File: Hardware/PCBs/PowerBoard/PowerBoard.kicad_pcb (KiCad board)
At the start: 2 copper layers, 24 parts, among them IC1 AZ34063UMTR-G1, IC2 LD29150DT33R, J1 Screw_Terminal_01x02, J2 Conn_01x04, J3 Screw_Terminal_01x02, J4 Conn_01x02, J5 Screw_Terminal_01x02, U1 L298HN

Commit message: PCB routed
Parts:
- added J6: Conn_01x02, Connector_PinSocket_2.54mm:PinSocket_1x02_P2.54mm_Vertical, F.Cu at (26.2, 76.6)
- IC1: footprint Package_SO:SOIC-8-1EP_3.9x4.9mm_P1.27mm_EP2.29x3mm_ThermalVias -> Package_SO:SOIC-8_3.9x4.9mm_P1.27mm
- IC2: footprint Package_TO_SOT_SMD:TO-252-2_TabPin1 -> Package_TO_SOT_SMD:TO-252-2
- moved L1 83.1 mm to (28.2, 56.6), turned to 180 degrees
- moved C5 77.0 mm to (34.9, 78.1), turned to 90 degrees
- moved C2 74.0 mm to (33.8, 55.0)
- moved Ctiming1 66.9 mm to (29.7, 61.6), turned to 180 degrees
- moved D3 65.9 mm to (37.1, 78.1), turned to 270 degrees
- moved C1 62.6 mm to (32.7, 68.0), turned to 180 degrees
- moved C4 61.9 mm to (54.7, 77.4), turned to 90 degrees
- moved Rsc1 58.2 mm to (42.0, 60.2), turned to 90 degrees
- moved R4 56.3 mm to (37.1, 73.6), turned to 90 degrees
- moved D2 54.5 mm to (55.0, 72.7)
- moved C3 48.9 mm to (55.8, 68.2), turned to 90 degrees
- moved J5 47.3 mm to (52.7, 56.6), turned to 180 degrees
- moved L2 45.7 mm to (48.8, 67.2)
- moved R2 43.3 mm to (37.1, 67.4), turned to 270 degrees
- moved U1 41.3 mm to (77.9, 74.6), turned to 180 degrees
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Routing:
- net GND: track 0.00 -> 147.2 mm
- net VCC: track 0.00 -> 74.8 mm, vias 0 -> 1
- net +3V3: track 0.00 -> 53.9 mm, vias 0 -> 1
- net Net-(J3-Pad2): track 0.00 -> 39.4 mm
- net Net-(J1-Pad1): track 0.00 -> 31.6 mm
- net Net-(J4-Pad2): track 0.00 -> 28.2 mm
- net +5V: track 0.00 -> 23.7 mm, vias 0 -> 1
- net +5F: track 0.00 -> 22.3 mm
- net Net-(J1-Pad2): track 0.00 -> 20.0 mm
- net Net-(J4-Pad1): track 0.00 -> 19.2 mm
- net Net-(J2-Pad4): track 0.00 -> 17.2 mm
- net Net-(J2-Pad2): track 0.00 -> 14.6 mm
- net Net-(J2-Pad3): track 0.00 -> 13.6 mm
- net Net-(D1-Pad2): track 0.00 -> 13.5 mm
- net Net-(J3-Pad1): track 0.00 -> 13.1 mm
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
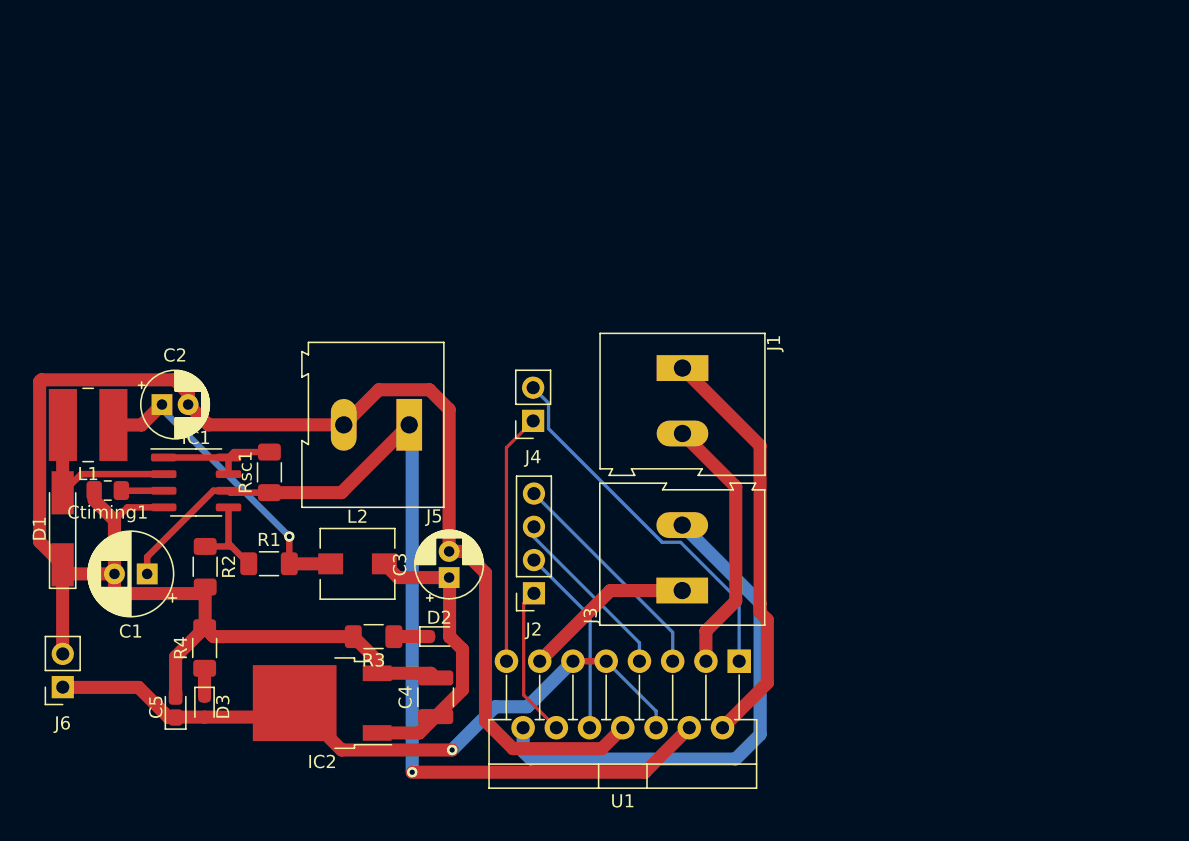
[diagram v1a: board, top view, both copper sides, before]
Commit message: Added ground planes and mounting holes
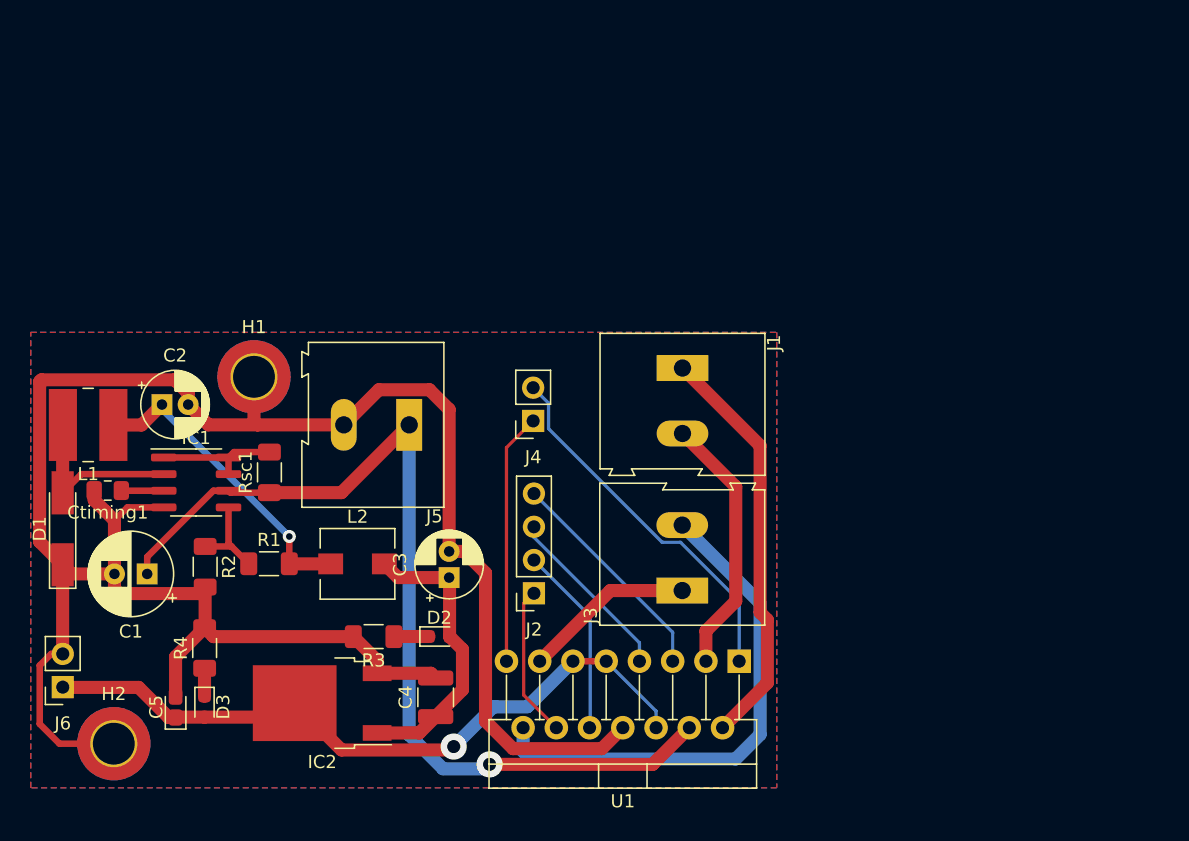
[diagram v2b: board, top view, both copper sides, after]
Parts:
- added H1: MountingHole_Pad, MountingHole:MountingHole_3.2mm_M3_DIN965_Pad_TopBottom, F.Cu at (40.9, 52.9)
- added H2: MountingHole_Pad, MountingHole:MountingHole_3.2mm_M3_DIN965_Pad_TopBottom, F.Cu at (30.1, 80.9)
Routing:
- net GND: track 147.2 -> 163.8 mm
- net VCC: track 74.8 -> 73.4 mm
- added copper zone on B.Cu, net GND
- added copper zone on F.Cu, net GND
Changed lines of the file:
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@@
   (general
     (thickness 1.6)
-    (drawings 0)
-    (tracks 145)
+    (drawings 6)
+    (tracks 160)
     (zones 0)
-    (modules 25)
+    (modules 27)
     (nets 22)
   )
@@
   )
   (setup
-    (last_trace_width 1)
+    (last_trace_width 0.5)
     (user_trace_width 0.5)
     (user_trace_width 1)
@@
     (via_min_size 0.4)
     (via_min_drill 0.3)
+    (user_via 1 0.5)
+    (user_via 2 1)
     (uvia_size 0.3)
     (uvia_drill 0.1)
@@
     (add_net "Net-(J4-Pad2)")
     (add_net VCC)
+  )
+  (module MountingHole:MountingHole_3.2mm_M3_DIN965_Pad_TopBottom (layer F.Cu)
+    (at 30.15 80.93)
+    (descr "Mounting Hole 3.2mm, M3, DIN965")
+    (tags "mounting hole 3.2mm m3 din965")
+    (attr virtual)
+    (fp_text reference H2 (at 0 -3.8) (layer F.SilkS)
+      (effects (font (size 1 1) (thickness 0.15)))
+    )
+    (fp_text value MountingHole_Pad (at 0 3.8) (layer F.Fab)
+      (effects (font (size 1 1) (thickness 0.15)))
+    )
+    (fp_text user %R (at 0.3 0) (layer F.Fab)
+      (effects (font (size 1 1) (thickness 0.15)))
+    )
+    (fp_circle (center 0 0) (end 2.8 0) (layer Cmts.User) (width 0.15))
+    (fp_circle (center 0 0) (end 3.05 0) (layer F.CrtYd) (width 0.05))
+    (pad 1 connect circle (at 0 0) (size 5.6 5.6) (layers B.Cu B.Mask)
+      (net 2 GND))
+    (pad 1 connect circle (at 0 0) (size 5.6 5.6) (layers F.Cu F.Mask)
+      (net 2 GND))
+    (pad 1 thru_hole circle (at 0 0) (size 3.6 3.6) (drill 3.2) (layers *.Cu *.Mask)
+      (net 2 GND))
+  )
+  (module MountingHole:MountingHole_3.2mm_M3_DIN965_Pad_TopBottom (layer F.Cu)
+    (at 40.86 52.9)
+    (descr "Mounting Hole 3.2mm, M3, DIN965")
+    (tags "mounting hole 3.2mm m3 din965")
+    (attr virtual)
+    (fp_text reference H1 (at 0 -3.8) (layer F.SilkS)
+      (effects (font (size 1 1) (thickness 0.15)))
+    )
+    (fp_text value MountingHole_Pad (at 0 3.8) (layer F.Fab)
+      (effects (font (size 1 1) (thickness 0.15)))
+    )
+    (fp_text user %R (at 0.3 0) (layer F.Fab)
+      (effects (font (size 1 1) (thickness 0.15)))
+    )
+    (fp_circle (center 0 0) (end 2.8 0) (layer Cmts.User) (width 0.15))
+    (fp_circle (center 0 0) (end 3.05 0) (layer F.CrtYd) (width 0.05))
+    (pad 1 connect circle (at 0 0) (size 5.6 5.6) (layers B.Cu B.Mask)
+      (net 2 GND))
+    (pad 1 connect circle (at 0 0) (size 5.6 5.6) (layers F.Cu F.Mask)
+      (net 2 GND))
+    (pad 1 thru_hole circle (at 0 0) (size 3.6 3.6) (drill 3.2) (layers *.Cu *.Mask)
+      (net 2 GND))
   )
   (module Connector_PinSocket_2.54mm:PinSocket_1x02_P2.54mm_Vertical (layer F.Cu)
@@
     )
   )
+  (gr_line (start 23.66 49.35) (end 81 49.35) (layer Dwgs.User) (width 0.15))
+  (gr_line (start 23.66 50.08) (end 23.66 49.35) (layer Dwgs.User) (width 0.15))
+  (gr_line (start 23.66 84.47) (end 23.66 50.08) (layer Dwgs.User) (width 0.15))
+  (gr_line (start 24.17 84.47) (end 23.66 84.47) (layer Dwgs.User) (width 0.15))
+  (gr_line (start 81 84.47) (end 24.17 84.47) (layer Dwgs.User) (width 0.15))
+  (gr_line (start 81 49.35) (end 81 84.47) (layer Dwgs.User) (width 0.15))
   (segment (start 47.54 61.75) (end 42.04 61.75) (width 1) (layer F.Cu) (net 1))
   (segment (start 52.72 56.57) (end 47.54 61.75) (width 1) (layer F.Cu) (net 1))
@@
   (segment (start 37.755 61.605) (end 38.915 61.605) (width 0.5) (layer F.Cu) (net 1))
   (segment (start 32.7 67.96) (end 32.7 66.66) (width 0.5) (layer F.Cu) (net 1))
-  (segment (start 74.12 79.71) (end 70.72 83.11) (width 1) (layer F.Cu) (net 1))
-  (segment (start 70.72 83.11) (end 52.95 83.11) (width 1) (layer F.Cu) (net 1))
-  (segment (start 52.95 83.11) (end 52.95 83.11) (width 1) (layer F.Cu) (net 1))
-  (via (at 52.95 83.11) (size 0.8) (drill 0.4) (layers F.Cu B.Cu) (net 1))
   (segment (start 52.95 56.8) (end 52.72 56.57) (width 1) (layer B.Cu) (net 1))
-  (segment (start 52.95 83.11) (end 52.95 56.8) (width 1) (layer B.Cu) (net 1))
+  (segment (start 71.319989 82.510011) (end 58.859989 82.510011) (width 1) (layer F.Cu) (net 1))
+  (segment (start 74.12 79.71) (end 71.319989 82.510011) (width 1) (layer F.Cu) (net 1))
+  (segment (start 58.859989 82.510011) (end 58.859989 82.510011) (width 1) (layer F.Cu) (net 1))
+  (via (at 58.859989 82.510011) (size 2) (drill 1) (layers F.Cu B.Cu) (net 1))
+  (segment (start 55.303999 82.850001) (end 58.519999 82.850001) (width 1) (layer B.Cu) (net 1))
+  (segment (start 58.519999 82.850001) (end 58.859989 82.510011) (width 1) (layer B.Cu) (net 1))
+  (segment (start 52.72 80.266002) (end 55.303999 82.850001) (width 1) (layer B.Cu) (net 1))
+  (segment (start 52.72 56.57) (end 52.72 80.266002) (width 1) (layer B.Cu) (net 1))
   (segment (start 37.38 56.57) (end 35.83 55.02) (width 1) (layer F.Cu) (net 2))
-  (segment (start 47.72 56.57) (end 37.38 56.57) (width 1) (layer F.Cu) (net 2))
   (segment (start 26.94 67.96) (end 26.24 67.26) (width 1) (layer F.Cu) (net 2))
   (segment (start 30.2 67.96) (end 26.94 67.96) (width 1) (layer F.Cu) (net 2))
@@
   (segment (start 56.90137 66.24) (end 58.549999 67.888629) (width 1) (layer F.Cu) (net 2))
   (segment (start 55.77 66.24) (end 56.90137 66.24) (width 1) (layer F.Cu) (net 2))
+  (segment (start 40.86 56.3) (end 41.13 56.57) (width 1) (layer F.Cu) (net 2))
+  (segment (start 40.86 52.9) (end 40.86 56.3) (width 1) (layer F.Cu) (net 2))
+  (segment (start 41.13 56.57) (end 37.38 56.57) (width 1) (layer F.Cu) (net 2))
+  (segment (start 47.72 56.57) (end 41.13 56.57) (width 1) (layer F.Cu) (net 2))
+  (segment (start 26 80.93) (end 30.15 80.93) (width 0.5) (layer F.Cu) (net 2))
+  (segment (start 24.49 79.42) (end 26 80.93) (width 0.5) (layer F.Cu) (net 2))
+  (segment (start 24.49 74.95) (end 24.49 79.42) (width 0.5) (layer F.Cu) (net 2))
+  (segment (start 25.37 74.07) (end 24.49 74.95) (width 0.5) (layer F.Cu) (net 2))
+  (segment (start 26.25 74.07) (end 25.37 74.07) (width 0.5) (layer F.Cu) (net 2))
   (segment (start 32.27 56.58) (end 33.83 55.02) (width 1) (layer F.Cu) (net 3))
   (segment (start 30.12 56.58) (end 32.27 56.58) (width 1) (layer F.Cu) (net 3))
@@
   (segment (start 43.56 67.18) (end 43.56 65.1) (width 0.5) (layer F.Cu) (net 3))
   (segment (start 43.56 65.1) (end 43.56 65.1) (width 0.5) (layer F.Cu) (net 3))
-  (via (at 43.56 65.1) (size 0.8) (drill 0.4) (layers F.Cu B.Cu) (net 3))
   (segment (start 33.83 55.37) (end 33.83 55.02) (width 0.5) (layer B.Cu) (net 3))
   (segment (start 43.56 65.1) (end 33.83 55.37) (width 0.5) (layer B.Cu) (net 3))
+  (segment (start 43.56 65.1) (end 43.56 65.1) (width 0.5) (layer F.Cu) (net 3))
+  (via (at 43.56 65.1) (size 1) (drill 0.5) (layers F.Cu B.Cu) (net 3))
   (segment (start 51.87 68.24) (end 55.77 68.24) (width 1) (layer F.Cu) (net 4))
   (segment (start 50.82 67.19) (end 51.87 68.24) (width 1) (layer F.Cu) (net 4))
@@
   (segment (start 37.08 78.9) (end 42.9 78.9) (width 1) (layer F.Cu) (net 5))
   (segment (start 67.77 74.63) (end 65.23 74.63) (width 0.5) (layer F.Cu) (net 5))
-  (segment (start 47.550001 81.410001) (end 55.999999 81.410001) (width 1) (layer F.Cu) (net 5))
   (segment (start 43.97 77.83) (end 47.550001 81.410001) (width 1) (layer F.Cu) (net 5))
-  (segment (start 55.999999 81.410001) (end 55.999999 81.410001) (width 1) (layer F.Cu) (net 5))
-  (via (at 55.999999 81.410001) (size 0.8) (drill 0.4) (layers F.Cu B.Cu) (net 5))
   (segment (start 61.750001 78.109999) (end 65.23 74.63) (width 1) (layer B.Cu) (net 5))
   (segment (start 59.300001 78.109999) (end 61.750001 78.109999) (width 1) (layer B.Cu) (net 5))
-  (segment (start 55.999999 81.410001) (end 59.300001 78.109999) (width 1) (layer B.Cu) (net 5))
   (segment (start 71.58 78.44) (end 71.58 79.71) (width 0.25) (layer B.Cu) (net 5))
   (segment (start 67.77 74.63) (end 71.58 78.44) (width 0.25) (layer B.Cu) (net 5))
+  (segment (start 59.300001 78.109999) (end 59.190001 78.109999) (width 1) (layer B.Cu) (net 5))
+  (segment (start 59.300001 78.109999) (end 59.160001 78.109999) (width 1) (layer B.Cu) (net 5))
+  (segment (start 59.160001 78.109999) (end 56.12 81.15) (width 1) (layer B.Cu) (net 5))
+  (segment (start 56.12 81.15) (end 56.12 81.15) (width 1) (layer B.Cu) (net 5))
+  (via (at 56.12 81.15) (size 2) (drill 1) (layers F.Cu B.Cu) (net 5))
+  (segment (start 55.859999 81.410001) (end 47.550001 81.410001) (width 1) (layer F.Cu) (net 5))
+  (segment (start 56.12 81.15) (end 55.859999 81.410001) (width 1) (layer F.Cu) (net 5))
   (segment (start 30.74 61.605) (end 30.725 61.59) (width 0.5) (layer F.Cu) (net 6))
   (segment (start 33.965 61.605) (end 30.74 61.605) (width 0.5) (layer F.Cu) (net 6))
@@
   (segment (start 77.93 70.024998) (end 73.450012 65.54501) (width 0.25) (layer B.Cu) (net 21))
   (segment (start 77.93 74.63) (end 77.93 70.024998) (width 0.25) (layer B.Cu) (net 21))
+  (zone (net 2) (net_name GND) (layer F.Cu) (hatch edge 0.508)
+    (connect_pads (clearance 0.508))
+    (min_thickness 0.254)
+    (fill yes (arc_segments 32) (thermal_gap 0.508) (thermal_bridge_width 0.508))
+    (polygon
+      (pts
+        (xy 80.8 84.3) (xy 23.8 84.3) (xy 23.8 49.5) (xy 80.8 49.5)
+      )
+    )
+  )
+  (zone (net 2) (net_name GND) (layer B.Cu) (hatch edge 0.508)
+    (connect_pads (clearance 0.508))
+    (min_thickness 0.254)
+    (fill yes (arc_segments 32) (thermal_gap 0.508) (thermal_bridge_width 0.508))
+    (polygon
+      (pts
+        (xy 80.8 84.3) (xy 23.8 84.3) (xy 23.8 49.5) (xy 80.8 49.5)
+      )
+    )
+  )
 )

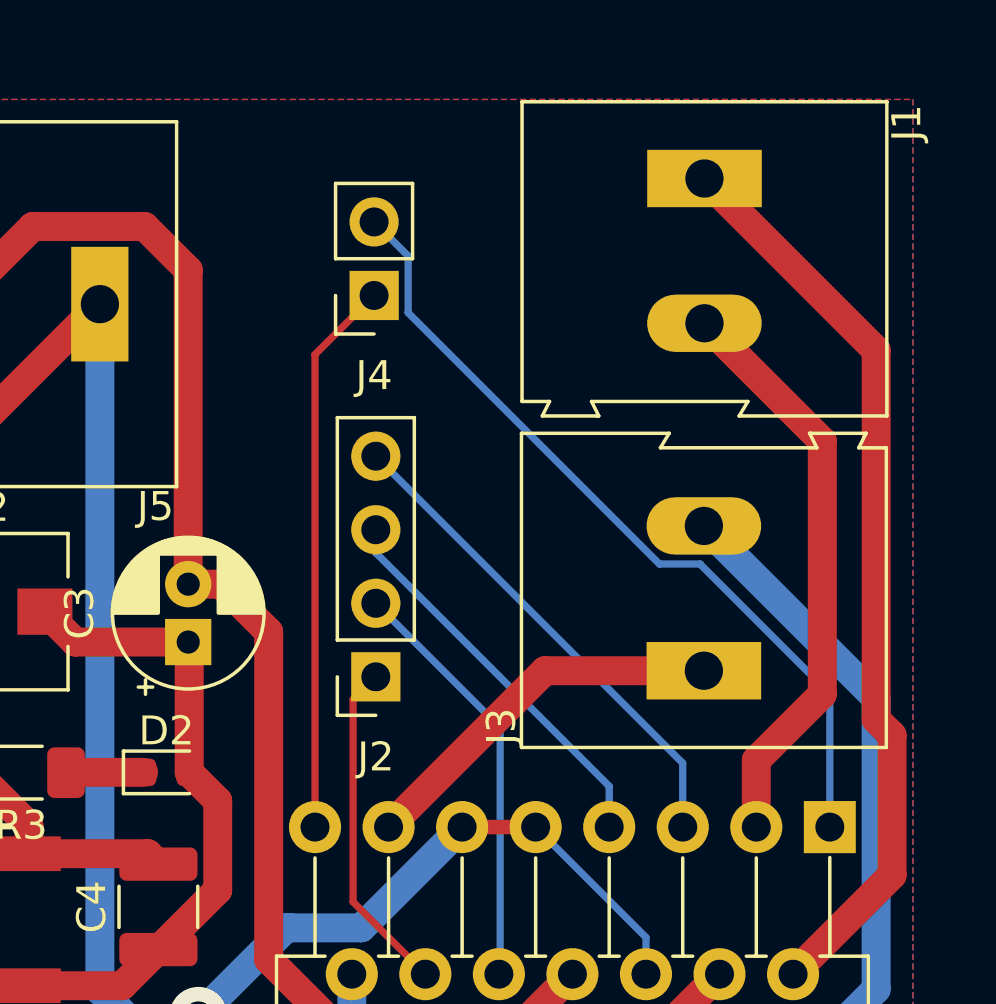
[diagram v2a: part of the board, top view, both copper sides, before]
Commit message: Added third mounting hole
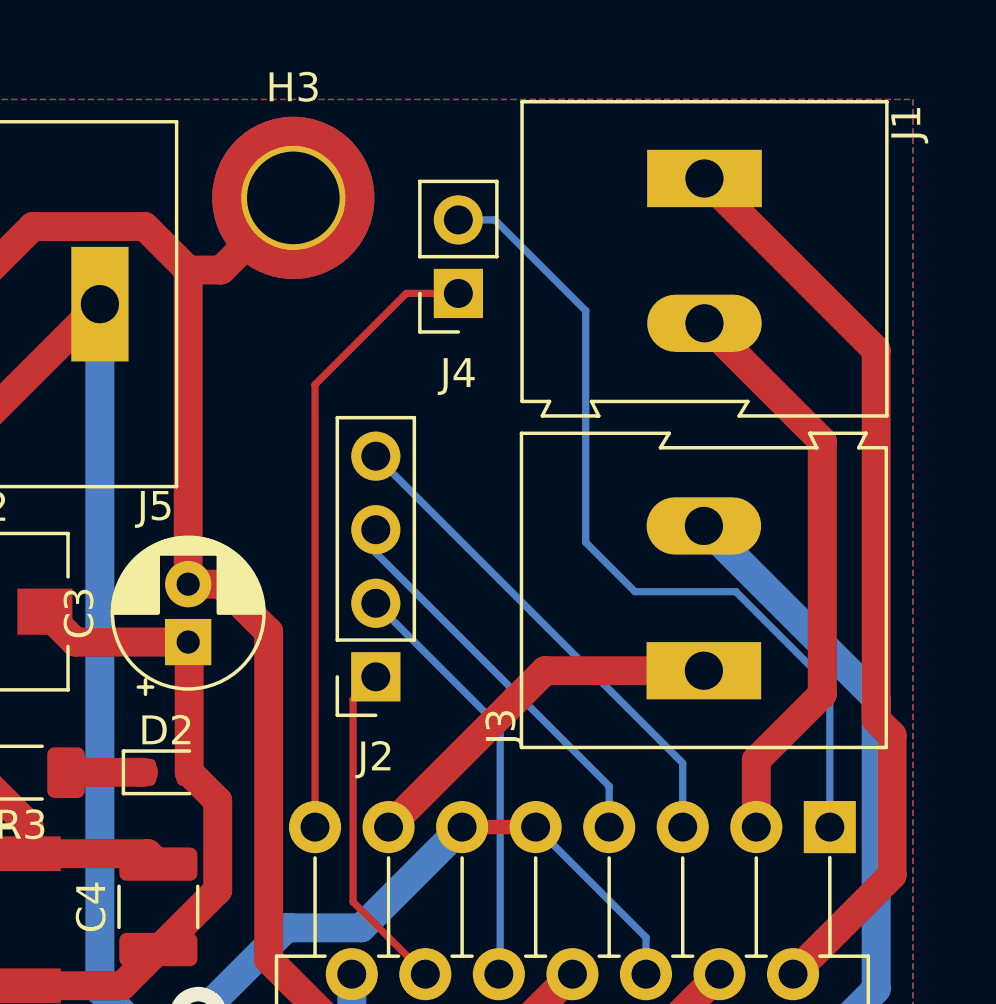
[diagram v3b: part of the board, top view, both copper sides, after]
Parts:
- added H3: MountingHole_Pad, MountingHole:MountingHole_3.2mm_M3_DIN965_Pad_TopBottom, F.Cu at (59.4, 52.9)
- moved J4 2.91 mm to (65.1, 56.2)
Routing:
- net GND: track 163.8 -> 168.5 mm
- net Net-(J4-Pad1): track 19.2 -> 21.5 mm
- net Net-(J4-Pad2): track 28.2 -> 29.1 mm
